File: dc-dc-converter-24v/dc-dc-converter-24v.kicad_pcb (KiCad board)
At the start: 2 copper layers, 54 parts, among them J1 24V, J2 12V, J3 GND, J4 GND, Q1 SQJA42EP, Q2 SQJA42EP, Q3 SQJA42EP, Q4 SQJA42EP, U1 LM5176

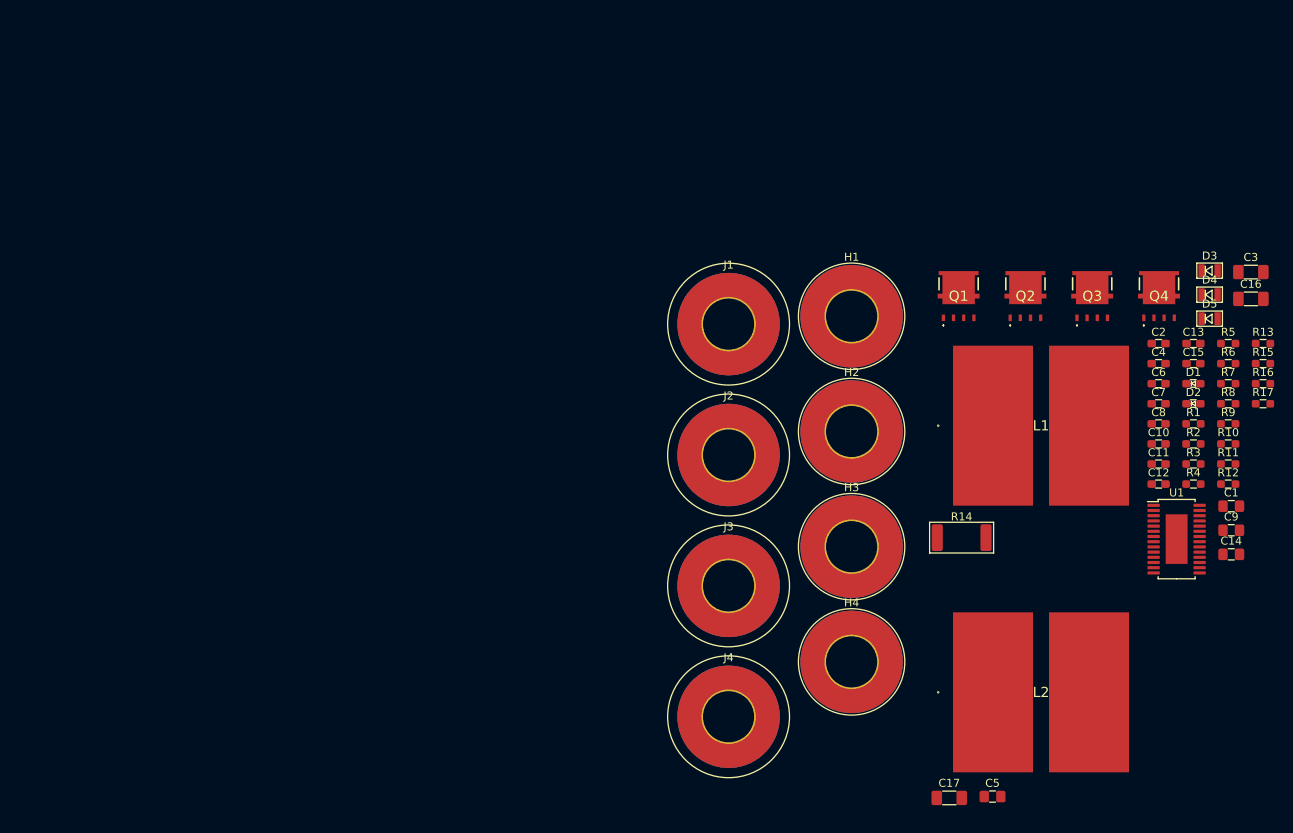
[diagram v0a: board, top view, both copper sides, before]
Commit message: add edge cuts
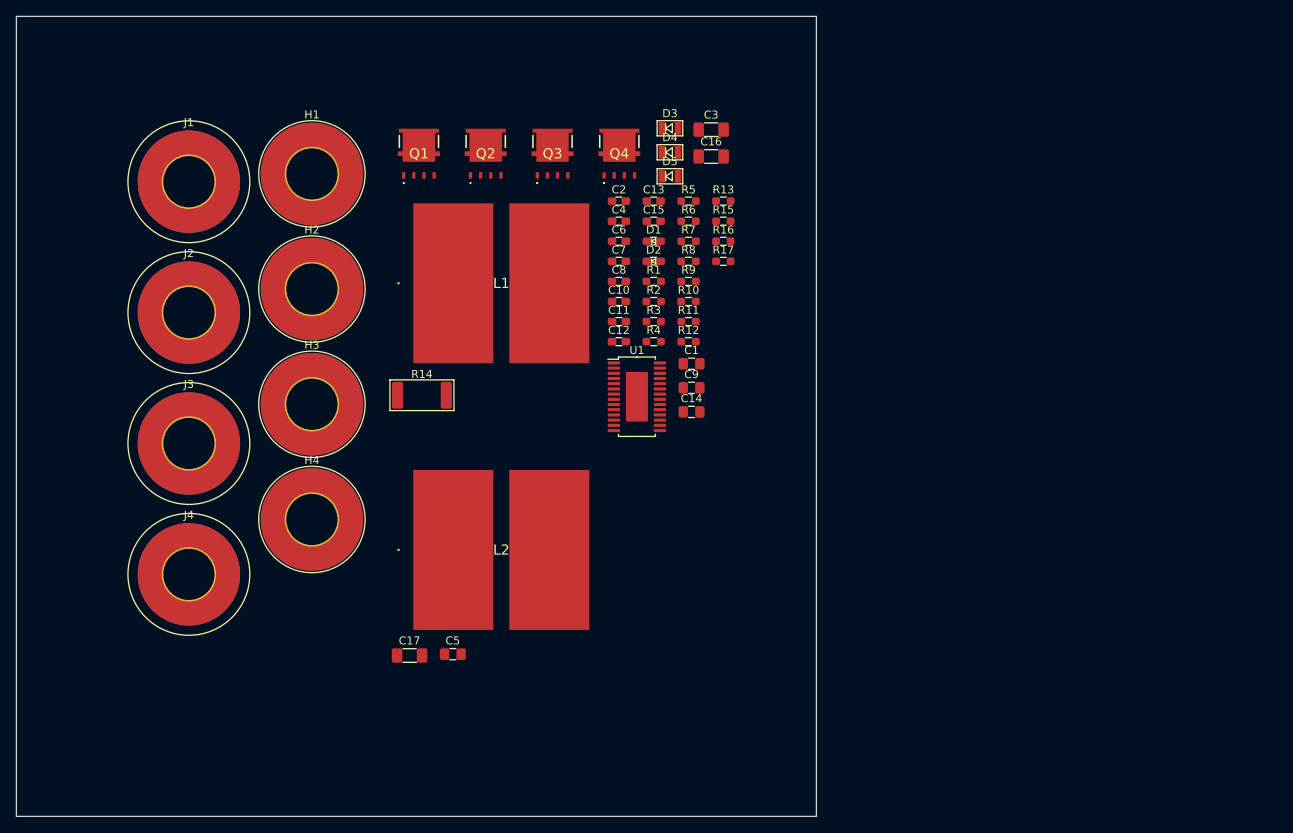
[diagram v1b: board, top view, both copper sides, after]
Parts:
- moved C10 69.8 mm to (95.3, 55.6)
- moved C11 69.8 mm to (95.3, 58.1)
- moved C12 69.8 mm to (95.3, 60.7)
- moved C16 69.8 mm to (106.8, 37.5)
- moved C2 69.8 mm to (95.3, 43.1)
- moved C3 69.8 mm to (106.8, 34.2)
- moved C4 69.8 mm to (95.3, 45.6)
- moved C5 69.8 mm to (74.6, 99.7)
- moved C6 69.8 mm to (95.3, 48.1)
- moved C7 69.8 mm to (95.3, 50.6)
- moved C8 69.8 mm to (95.3, 53.1)
- moved D3 69.8 mm to (101.7, 34.0)
- moved D4 69.8 mm to (101.7, 37.0)
- moved D5 69.8 mm to (101.7, 40.0)
- moved H1 69.8 mm to (56.9, 39.7)
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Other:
- board outline added: 100 x 100 mm
